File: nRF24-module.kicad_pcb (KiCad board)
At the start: 2 copper layers, 29 parts, among them P1 CONN_02X04, U1 STM32F302C8T, U2 SN65HVD256, U3 MCP1703, X1 16MHz 10ppm

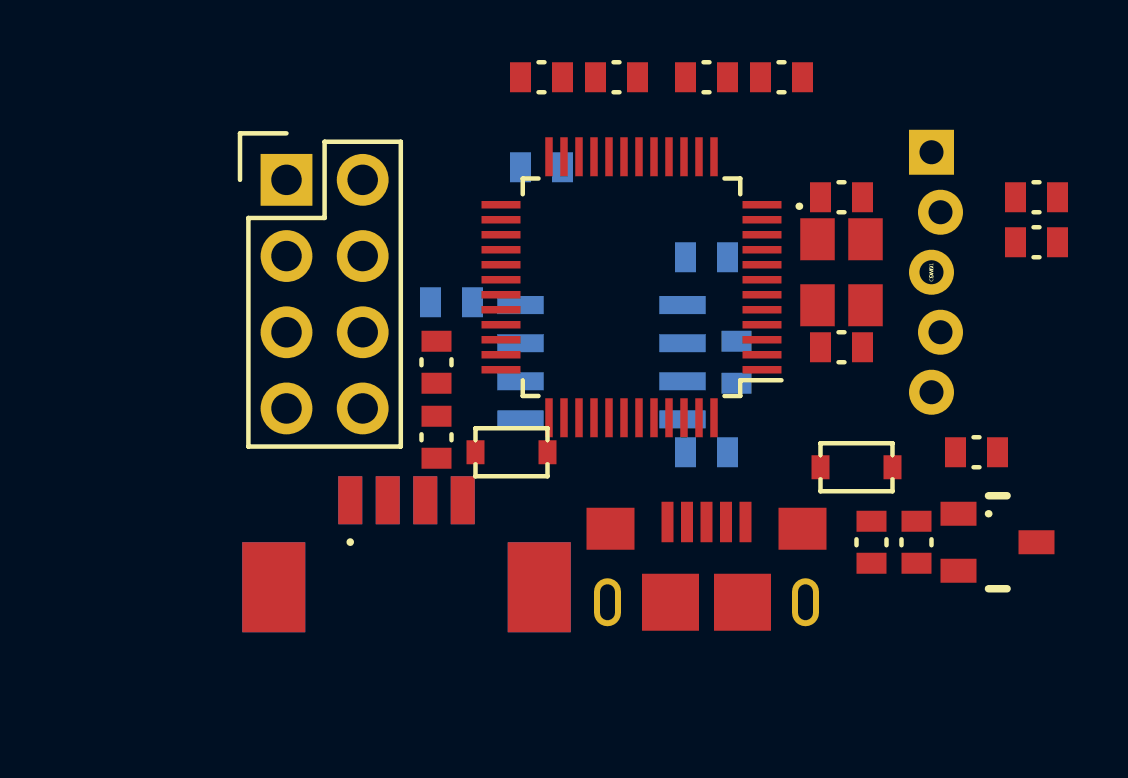
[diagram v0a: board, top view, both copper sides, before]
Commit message: Routing, change pins, add debug UART
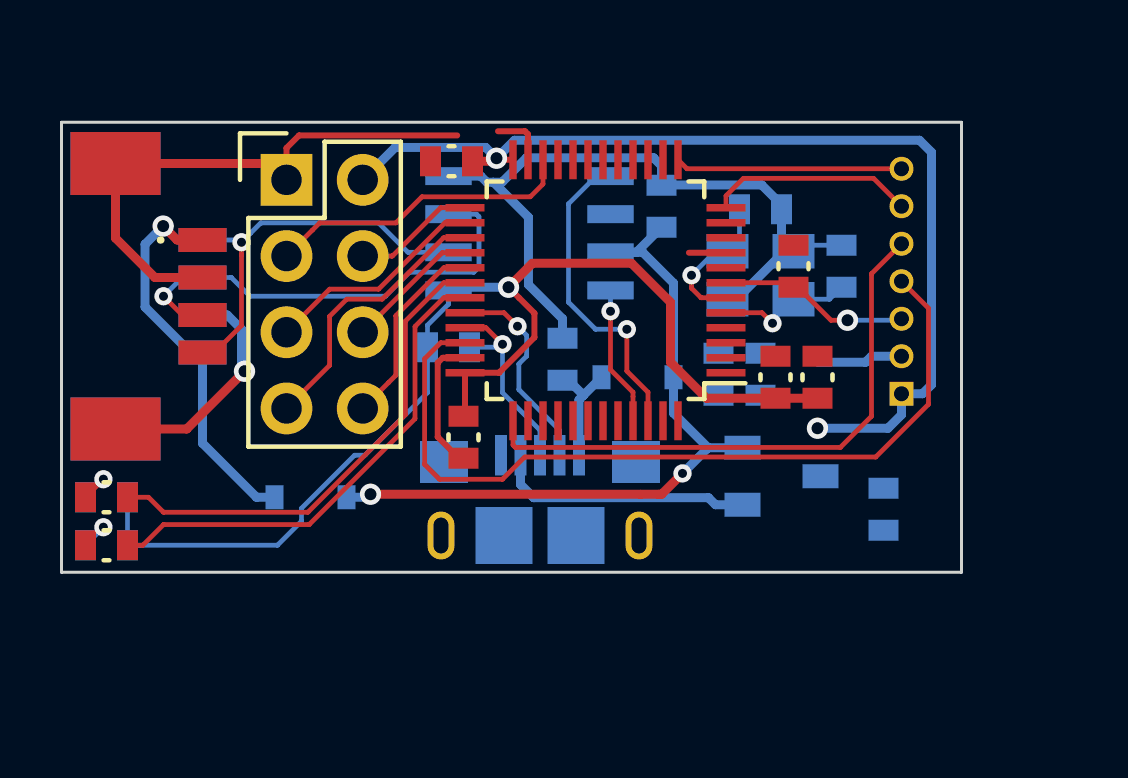
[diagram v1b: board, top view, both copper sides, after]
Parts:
- removed R1: 10k, _std:_0603
- C1, C2, C3, C5: moved to F.Cu
- C10, C11, C12, C6, C7, C9, CONN2, D3, D4, R2, R3, R4, U3, X1: moved to B.Cu
- CONN1: value SWD -> CONN_01X07; footprint _connectors:_Pin2mm_5z -> Connectors_Molex:Connector_Molex_PicoBlade_53047-0710; moved to B.Cu
- moved R2 27.4 mm to (21.5, 33.1), turned to 0 degrees
- moved D1 25.4 mm to (21.5, 33.1), turned to 180 degrees
- moved D2 22.0 mm to (21.5, 31.5)
- moved R3 20.2 mm to (21.5, 31.5)
- moved D3 18.2 mm to (28.3, 31.5)
- moved CONN3 13.7 mm to (21.8, 24.8), turned to 90 degrees
- moved CONN4 13.7 mm to (21.8, 24.8), turned to 270 degrees
- moved C2 12.9 mm to (33.0, 20.3), turned to 180 degrees
- moved C5 10.5 mm to (43.8, 27.5), turned to 90 degrees
- moved C9 8.66 mm to (41.9, 27.4)
- moved C4 8.14 mm to (44.4, 23.8), turned to 90 degrees
- moved U3 7.21 mm to (42.7, 31.8), turned to 90 degrees
- moved C10 6.71 mm to (43.3, 27.4)
- moved CONN2 5.98 mm to (36.0, 32.8), turned to 180 degrees
- moved C8 5.77 mm to (40.0, 21.8)
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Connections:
- D1 pad 1: GND -> /RX_LED
- D2 pad 1: GND -> /TX_LED
- R2 pad 1: /RX_LED -> Net-(D1-Pad2)
- R2 pad 2: Net-(D1-Pad2) -> VCC
- R3 pad 1: /TX_LED -> Net-(D2-Pad2)
- R3 pad 2: Net-(D2-Pad2) -> VCC
- U1 pad 10: /RX_LED -> (no net)
- U1 pad 11: /TX_LED -> (no net)
- U1 pad 12: (no net) -> /UART2_TX
- U1 pad 13: (no net) -> /UART2_RX
- U1 pad 21: /nRF_IRQ -> (no net)
- U1 pad 29: (no net) -> /nRF_IRQ
- U1 pad 30: (no net) -> /TX_LED
- U1 pad 31: (no net) -> /RX_LED
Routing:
- net VCC: track 0.00 -> 74.9 mm, vias 0 -> 3
- net GND: track 0.00 -> 69.8 mm, vias 0 -> 1
- net /SWDIO: track 0.00 -> 27.6 mm
- net +5V: track 0.00 -> 24.9 mm, vias 0 -> 2
- net /SWCLK: track 0.00 -> 19.4 mm
- net /RX_LED: track 0.00 -> 16.5 mm
- net /TX_LED: track 0.00 -> 16.5 mm
- net Net-(CONN3-Pad3): track 0.00 -> 15.7 mm, vias 0 -> 1
- net (no net): track 0.00 -> 15.0 mm
- net Net-(CONN3-Pad4): track 0.00 -> 13.4 mm, vias 0 -> 1
- net /V_CAN_BUS: track 0.00 -> 13.2 mm, vias 0 -> 1
- net /CAN1_TX: track 0.00 -> 10.7 mm, vias 0 -> 1
- net /nRF_CE: track 0.00 -> 10.4 mm
- net /SPI2_MISO: track 0.00 -> 9.26 mm
- net /UART2_RX: track 0.00 -> 7.57 mm
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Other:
- board outline added: 30 x 15 mm
- net class Default: clearance 0.2 -> 0.16; trace_width 0.25 -> 0.16; via_dia 0.6 -> 0.61; via_drill 0.4 -> 0.3
- rule trace_clearance: 0.2 -> 0.16
- rule trace_min: 0.2 -> 0.1525
- rule via_min_size: 0.4 -> 0.61

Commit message: Routing almost finished, add capacitor to nRF24 VCC
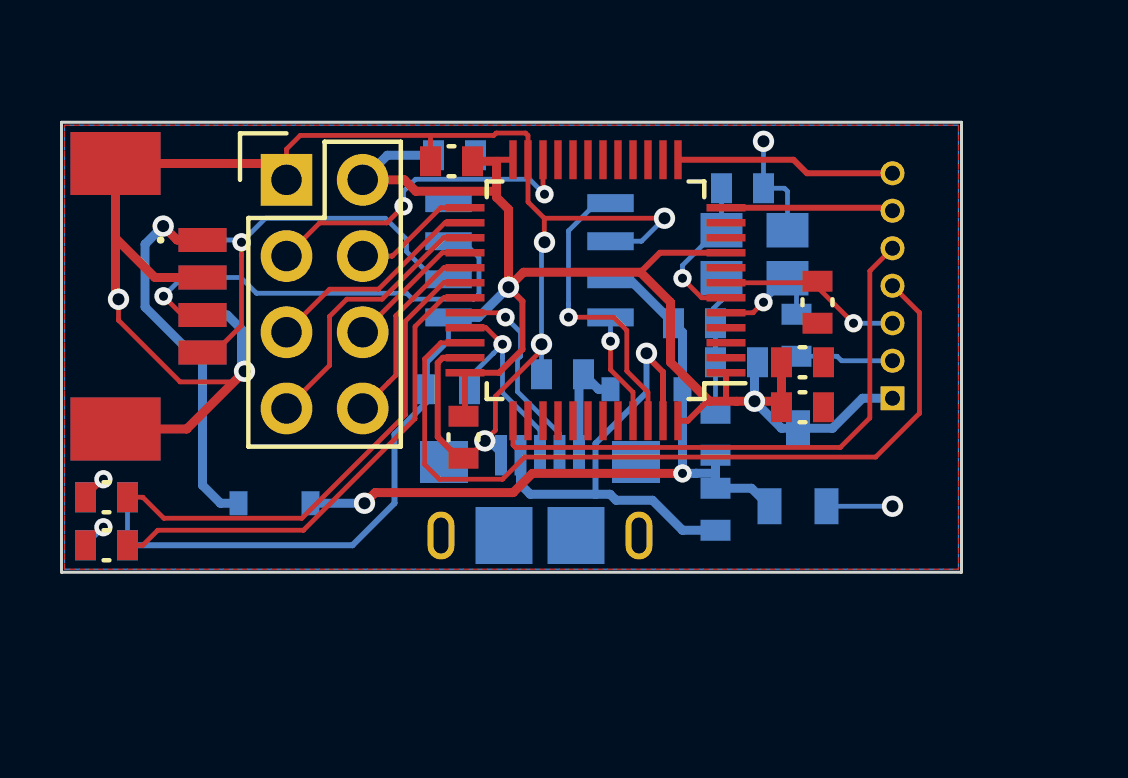
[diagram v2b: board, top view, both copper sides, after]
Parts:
- added C13: 1uF, _std:_0603, B.Cu at (33.1, 20.1)
- moved C12 6.93 mm to (42.5, 27.0), turned to 180 degrees
- moved C9 4.50 mm to (41.8, 31.9), turned to 270 degrees
- moved C8 4.05 mm to (41.1, 25.7), turned to 0 degrees
- moved U3 2.80 mm to (45.5, 31.8), turned to 180 degrees
- moved C7 2.75 mm to (44.5, 26.1), turned to 90 degrees
- moved C10 2.50 mm to (41.8, 29.4)
- moved C4 1.44 mm to (45.2, 25.0), turned to 270 degrees
- moved R4 1.40 mm to (32.9, 27.9)
- moved D3 1.22 mm to (27.1, 31.7)
- moved C1 1.12 mm to (44.7, 28.5), turned to 0 degrees
- moved C5 1.03 mm to (44.7, 27.0), turned to 0 degrees
- moved C6 0.92 mm to (42.7, 21.2)
- moved U2 0.90 mm to (35.6, 23.6)
- moved X1 0.73 mm to (43.1, 23.4)
- moved C11 0.50 mm to (36.7, 27.4), turned to 180 degrees
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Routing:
- net GND: track 69.8 -> 92.5 mm, vias 1 -> 9
- net VCC: track 74.9 -> 65.7 mm, vias 3 -> 2
- net /UART2_TX: track 6.88 -> 5.59 mm
- net /nRF_CE: track 10.4 -> 11.3 mm, vias 0 -> 2
- net /CAN1_RX: track 4.66 -> 3.76 mm
- net /USB_D+: track 6.84 -> 7.65 mm
- net Net-(CONN3-Pad4): track 13.4 -> 14.1 mm
- net Net-(C7-Pad2): track 4.55 -> 3.85 mm
- net /CAN1_TX: track 10.7 -> 10.1 mm
- net Net-(CONN3-Pad3): track 15.7 -> 15.2 mm
- net Net-(C6-Pad2): track 4.81 -> 5.34 mm
- added copper zone on B.Cu, net GND
- added copper zone on F.Cu, net GND
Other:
- rule pad_to_mask_clearance: 0 -> 0.13

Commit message: Add mounting holes
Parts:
- added _M2: VAL**, _mech:_M2, F.Cu at (47.5, 36.3)
- added _M2: VAL**, _mech:_M2, F.Cu at (22.7, 36.5)
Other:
- board size 30 x 15 mm -> 30 x 19.8 mm
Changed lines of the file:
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@@
 (kicad_pcb (version 4) (host pcbnew 4.0.1-stable)
   (general
-    (links 93)
+    (links 0)
     (no_connects 9)
-    (area 19.949999 18.949999 50.050001 34.050001)
+    (area 19.949999 14.149999 50.050001 38.850001)
     (thickness 1.6)
-    (drawings 6)
+    (drawings 12)
     (tracks 334)
     (zones 0)
-    (modules 29)
+    (modules 31)
     (nets 30)
   )
@@
     (mod_text_size 1 1)
     (mod_text_width 0.15)
-    (pad_size 1.5 1.5)
-    (pad_drill 0.6)
+    (pad_size 4.45 4.45)
+    (pad_drill 2.2)
     (pad_to_mask_clearance 0.13)
     (solder_mask_min_width 0.1)
@@
     )
   )
-  (gr_line (start 50 34) (end 20 34) (layer Edge.Cuts) (width 0.1))
-  (gr_line (start 50 19) (end 50 34) (layer Edge.Cuts) (width 0.1))
+  (module _mech:_M2 (layer F.Cu)
+    (at 47.5 36.3)
+    (fp_text reference _M2 (at 0 -1.27) (layer F.SilkS)
+      (effects (font (size 1 1) (thickness 0.15)))
+    )
+    (fp_text value VAL** (at 0 1.27) (layer F.SilkS)
+      (effects (font (size 1 1) (thickness 0.15)))
+    )
+    (pad 1 thru_hole circle (at 0 0) (size 4.45 4.45) (drill 2.2) (layers *.Cu *.Mask F.SilkS))
+  )
+  (module _mech:_M2 (layer F.Cu)
+    (at 22.7 36.5)
+    (fp_text reference _M2 (at 0 -1.27) (layer F.SilkS)
+      (effects (font (size 1 1) (thickness 0.15)))
+    )
+    (fp_text value VAL** (at 0 1.27) (layer F.SilkS)
+      (effects (font (size 1 1) (thickness 0.15)))
+    )
+    (pad 1 thru_hole circle (at -0.2 -0.2) (size 4.45 4.45) (drill 2.2) (layers *.Cu *.Mask F.SilkS))
+  )
+  (gr_arc (start 44.5 34.5) (end 44.5 34) (angle 90) (layer Edge.Cuts) (width 0.1))
+  (gr_arc (start 25.5 34.5) (end 25 34.5) (angle 90) (layer Edge.Cuts) (width 0.1))
+  (gr_line (start 25 36.3) (end 25 34.5) (layer Edge.Cuts) (width 0.1))
+  (gr_arc (start 22.5 36.3) (end 25 36.3) (angle 180) (layer Edge.Cuts) (width 0.1))
+  (gr_arc (start 47.5 36.3) (end 50 36.3) (angle 180) (layer Edge.Cuts) (width 0.1))
+  (gr_line (start 45 34.5) (end 45 36.3) (layer Edge.Cuts) (width 0.1))
+  (gr_line (start 44.5 34) (end 25.5 34) (layer Edge.Cuts) (width 0.1))
+  (gr_line (start 50 19) (end 50 36.3) (layer Edge.Cuts) (width 0.1))
   (gr_line (start 20 19) (end 50 19) (layer Edge.Cuts) (width 0.1))
   (dimension 30 (width 0.3) (layer Cmts.User)
@@
     (arrow2b (pts (xy 20 40) (xy 21.126504 39.413579)))
   )
-  (gr_line (start 20 34) (end 20 19) (layer Edge.Cuts) (width 0.1))
+  (gr_line (start 20 36.3) (end 20 19) (layer Edge.Cuts) (width 0.1))
   (dimension 15 (width 0.3) (layer Cmts.User)
     (gr_text "15.000 mm" (at 14.54919 26.468506 90) (layer Cmts.User)

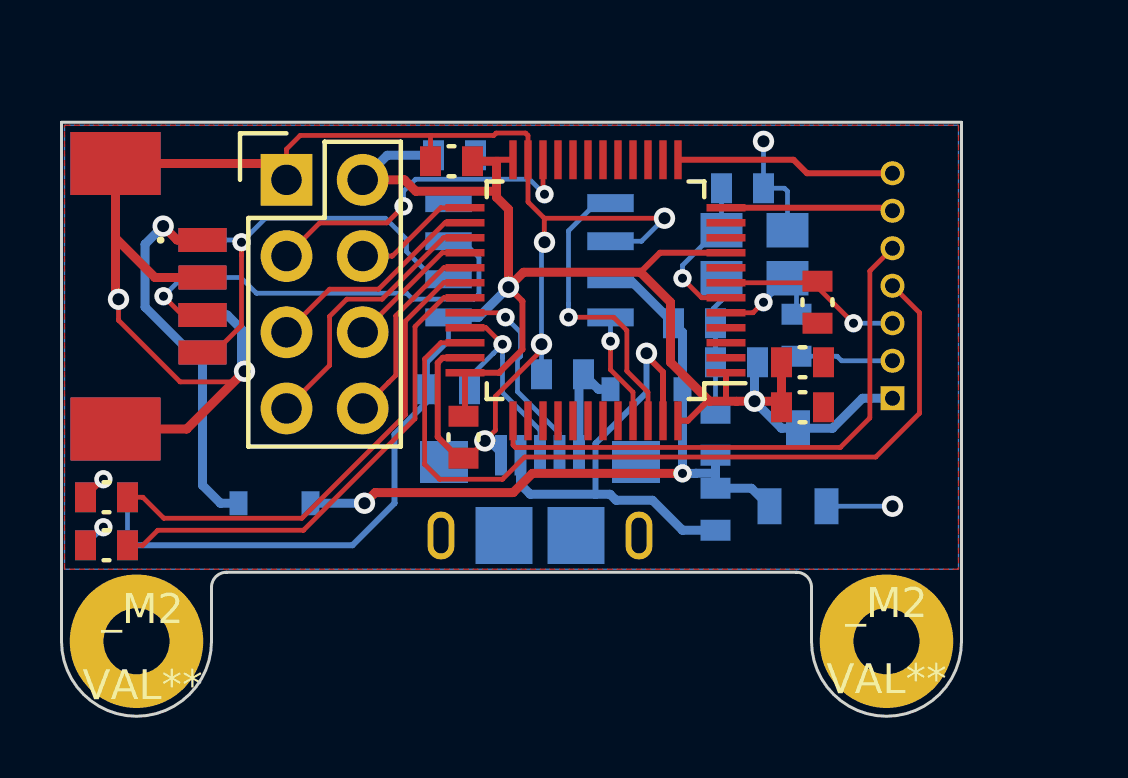
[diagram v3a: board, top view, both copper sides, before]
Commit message: Change LED polarity, optimize routing
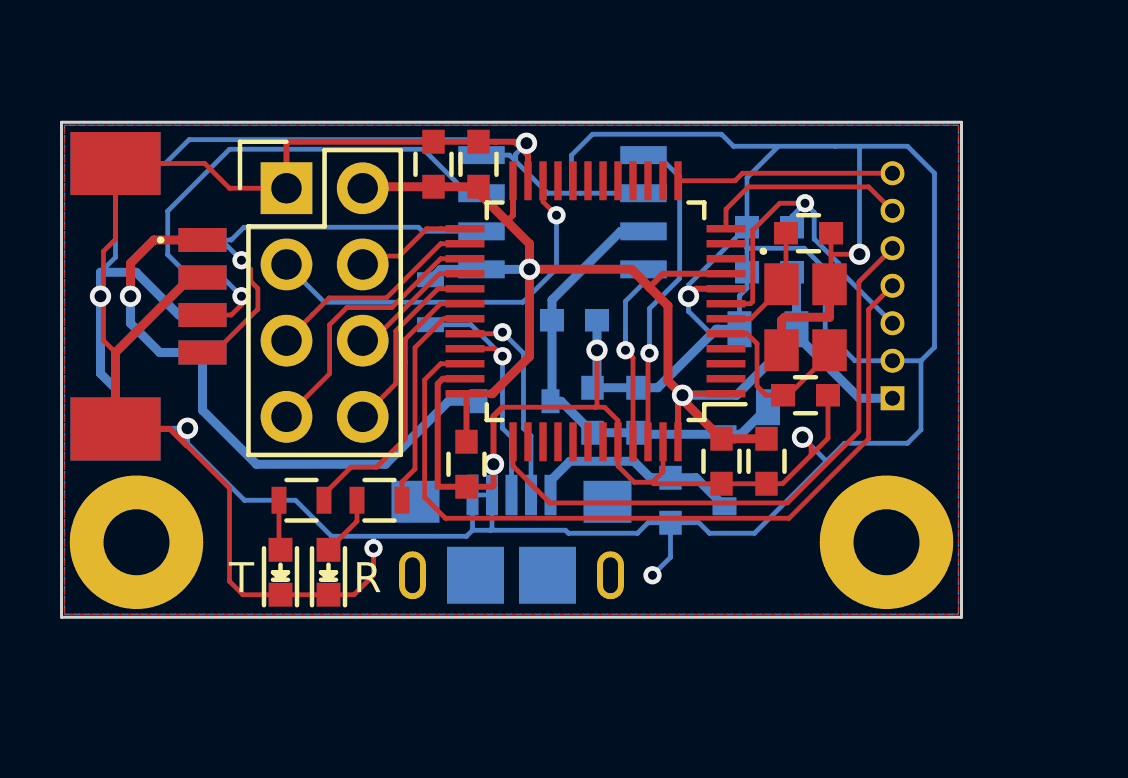
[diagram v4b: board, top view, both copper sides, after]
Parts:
- C1, C10, C11, C12, C2, C3, C5, C8, C9: footprint _std:_0603 -> Capacitors_SMD:C_0603
- C13, C6, C7: footprint _std:_0603 -> Capacitors_SMD:C_0603; moved to F.Cu
- C4: footprint _std:_0603 -> Capacitors_SMD:C_0603; moved to B.Cu
- D1, D2: footprint _std:_0603 -> LEDs:LED-0603
- R2, R3: footprint _std:_0603 -> Resistors_SMD:R_0603; moved to F.Cu
- R4: footprint _std:_0603 -> Resistors_SMD:R_0603
- U3: footprint _std:_SOT23-3 -> _div:_MCP1703-SOT-23A
- X1: moved to F.Cu
- moved R2 9.22 mm to (30.6, 31.6), turned to 180 degrees
- moved D3 8.69 mm to (35.1, 28.3)
- moved D1 7.45 mm to (28.9, 34.0), turned to 90 degrees
- moved U3 6.57 mm to (42.6, 25.9), turned to 0 degrees
- moved R3 6.50 mm to (28.0, 31.6), turned to 180 degrees
- moved D2 6.32 mm to (27.3, 34.0), turned to 90 degrees
- moved C11 5.53 mm to (40.3, 31.6), turned to 270 degrees
- moved C9 4.20 mm to (39.2, 28.6), turned to 90 degrees
- moved C10 4.18 mm to (37.7, 28.6)
- moved C8 4.00 mm to (37.1, 25.6)
- moved D4 3.75 mm to (42.1, 30.6), turned to 270 degrees
- moved C5 3.51 mm to (43.5, 30.3), turned to 270 degrees
- moved _M2 3.30 mm to (22.7, 33.2)
- moved _M2 3.30 mm to (47.5, 33.0)
- moved C1 3.24 mm to (42.0, 30.3), turned to 270 degrees
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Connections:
- CONN2 pad 6: Net-(CONN2-Pad6) -> (no net)
- D1 pad 1: /RX_LED -> GND
- D2 pad 1: /TX_LED -> GND
- R2 pad 1: Net-(D1-Pad2) -> /RX_LED
- R2 pad 2: VCC -> Net-(D1-Pad2)
- R3 pad 1: Net-(D2-Pad2) -> /TX_LED
- R3 pad 2: VCC -> Net-(D2-Pad2)
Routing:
- net GND: track 92.5 -> 206.8 mm, vias 9 -> 10
- net VCC: track 65.7 -> 47.9 mm
- net +5V: track 24.9 -> 15.5 mm, vias 2 -> 0
- net /RX_LED: track 16.5 -> 7.33 mm
- net /V_CAN_BUS: track 12.9 -> 20.3 mm
- net /TX_LED: track 16.6 -> 9.47 mm
- net /NRST: track 6.34 -> 11.9 mm
- net Net-(CONN3-Pad3): track 15.2 -> 18.8 mm
- net /V_USB: track 3.87 -> 7.17 mm
- net /CAN1_RX: track 3.76 -> 6.10 mm
- net Net-(C7-Pad2): track 3.85 -> 5.82 mm, vias 1 -> 0
- net /nRF_CE: track 11.3 -> 13.1 mm, vias 2 -> 1
- net /UART2_TX: track 5.59 -> 6.98 mm
- net Net-(CONN3-Pad4): track 14.1 -> 15.4 mm
- net /SWCLK: track 19.1 -> 20.4 mm
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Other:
- board size 30 x 19.8 mm -> 30 x 16.5 mm
- board text added: "R"
- board text added: "T"
